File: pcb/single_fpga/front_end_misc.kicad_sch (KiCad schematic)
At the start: 20 parts, among them Q1 2N7002, Q2 2N7002, Q3 2N7002

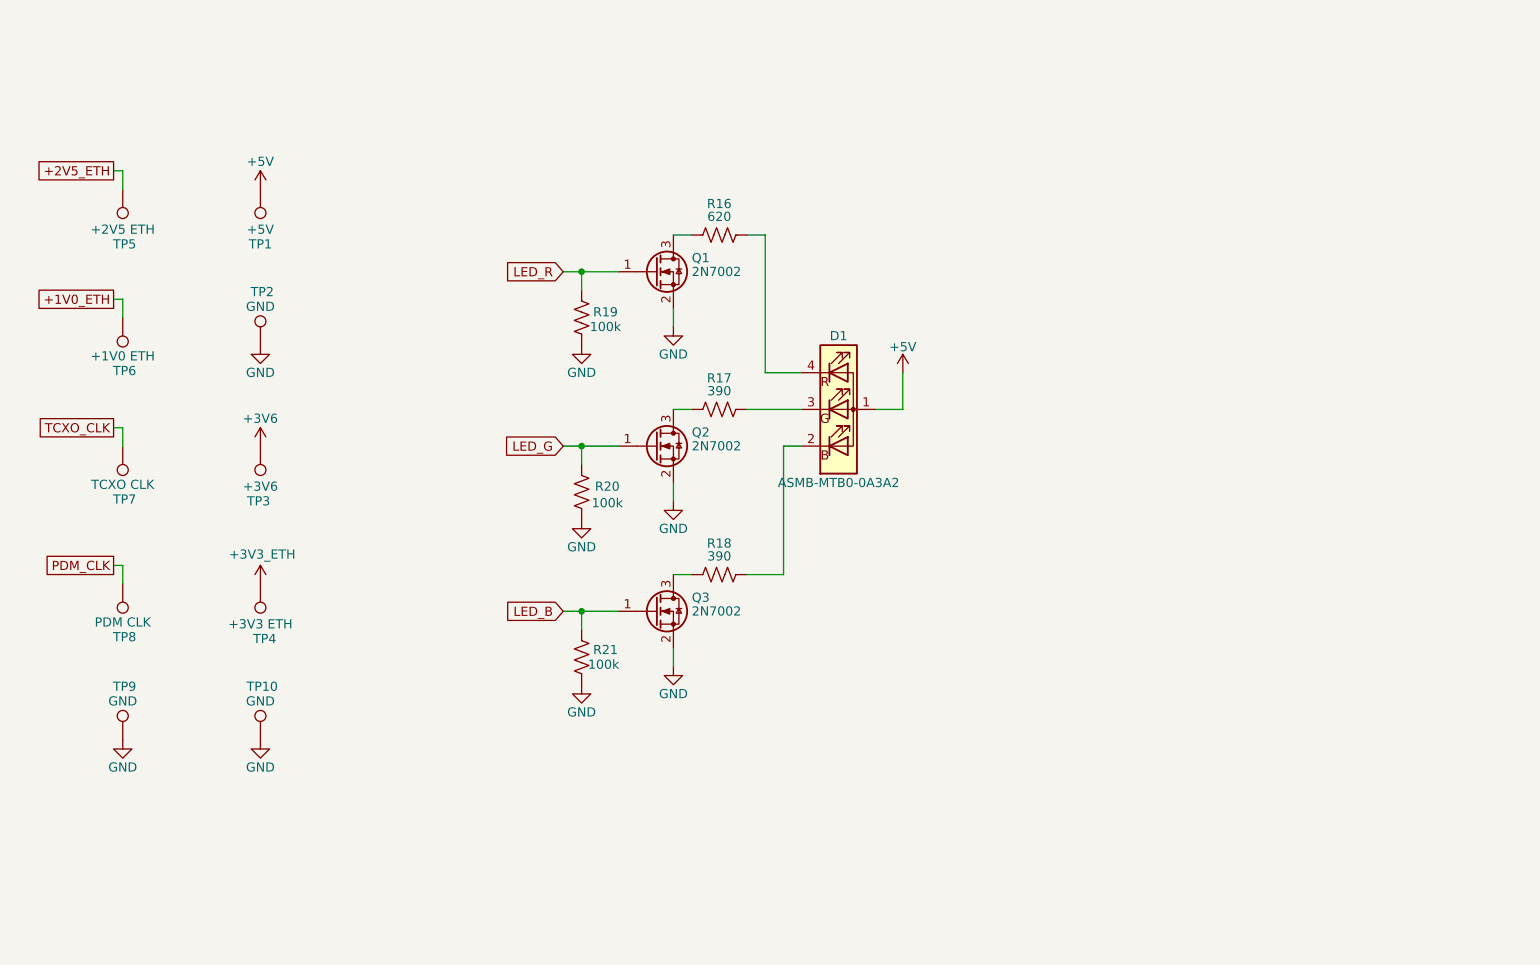
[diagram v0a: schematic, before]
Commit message: Added more stitching caps and vias. Carved +5V island in In2.Cu and renamed.
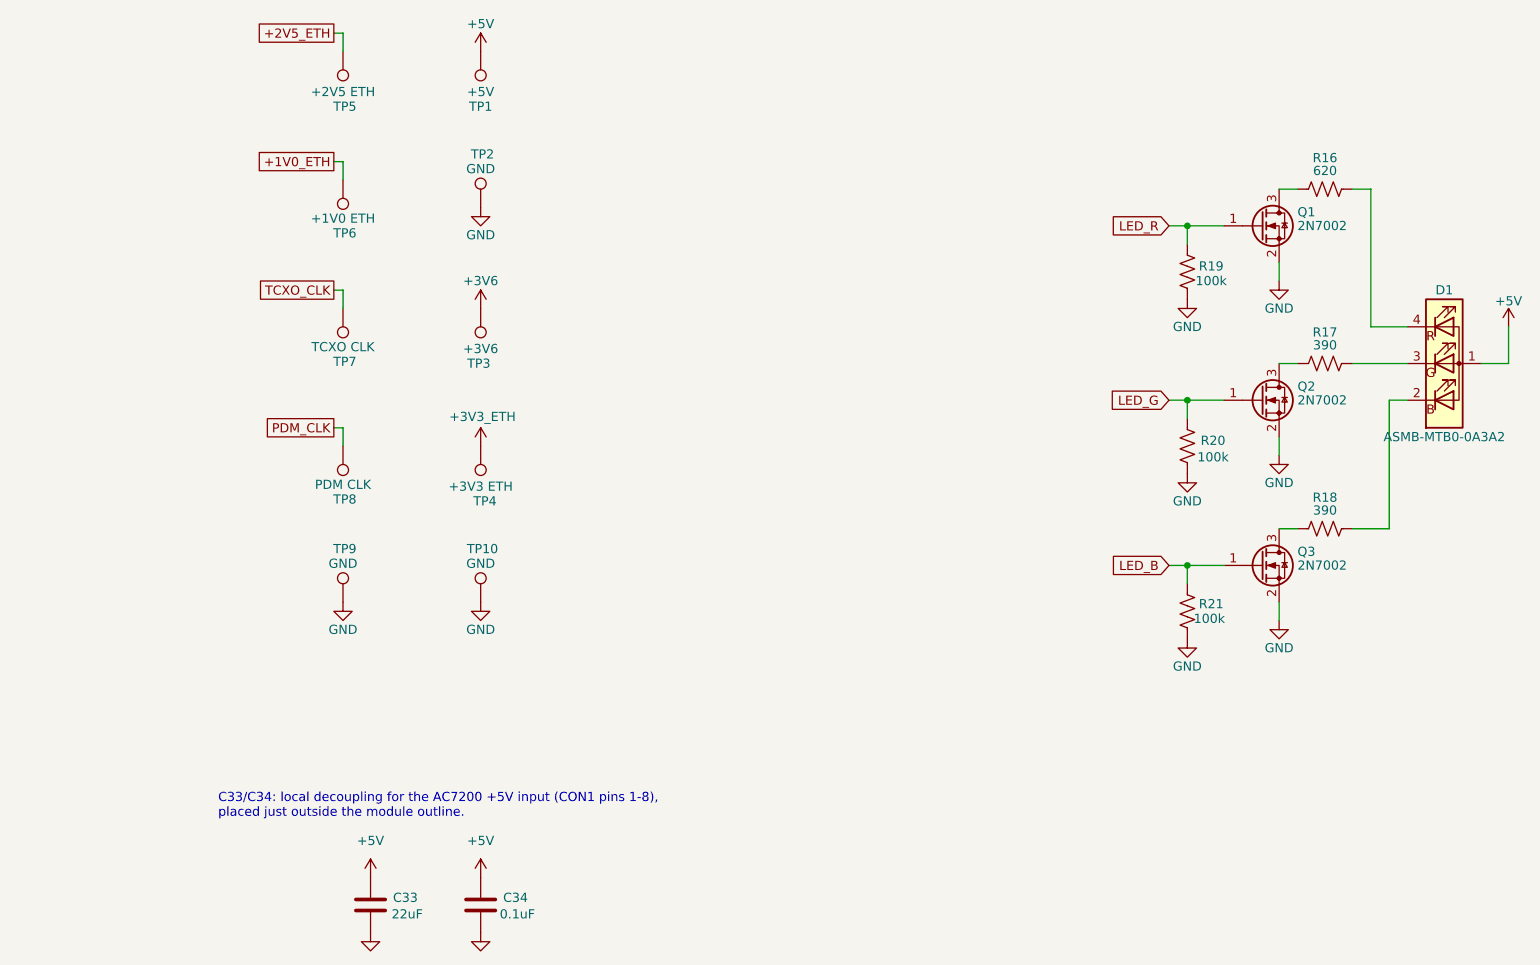
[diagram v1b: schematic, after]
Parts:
- added C33: 22uF, Capacitor_SMD:C_0805_2012Metric, symbol Device:C
- added C34: 0.1uF, Capacitor_SMD:C_0402_1005Metric, symbol Device:C
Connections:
- net +5V: now also C33.1, C34.1
- net GND: now also C33.2, C34.2
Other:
- note added: "C33/C34: local decoupling for the AC7200 +5V input (CON1 pins 1-8), placed just outside the module outline."
- moved on the sheet: D1, Q1, Q2, Q3, R16, R17, R18, R19, R20, R21, TP1, TP10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
